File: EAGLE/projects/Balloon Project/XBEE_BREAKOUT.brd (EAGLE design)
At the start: 62.2 x 64.4 mm, 2 parts

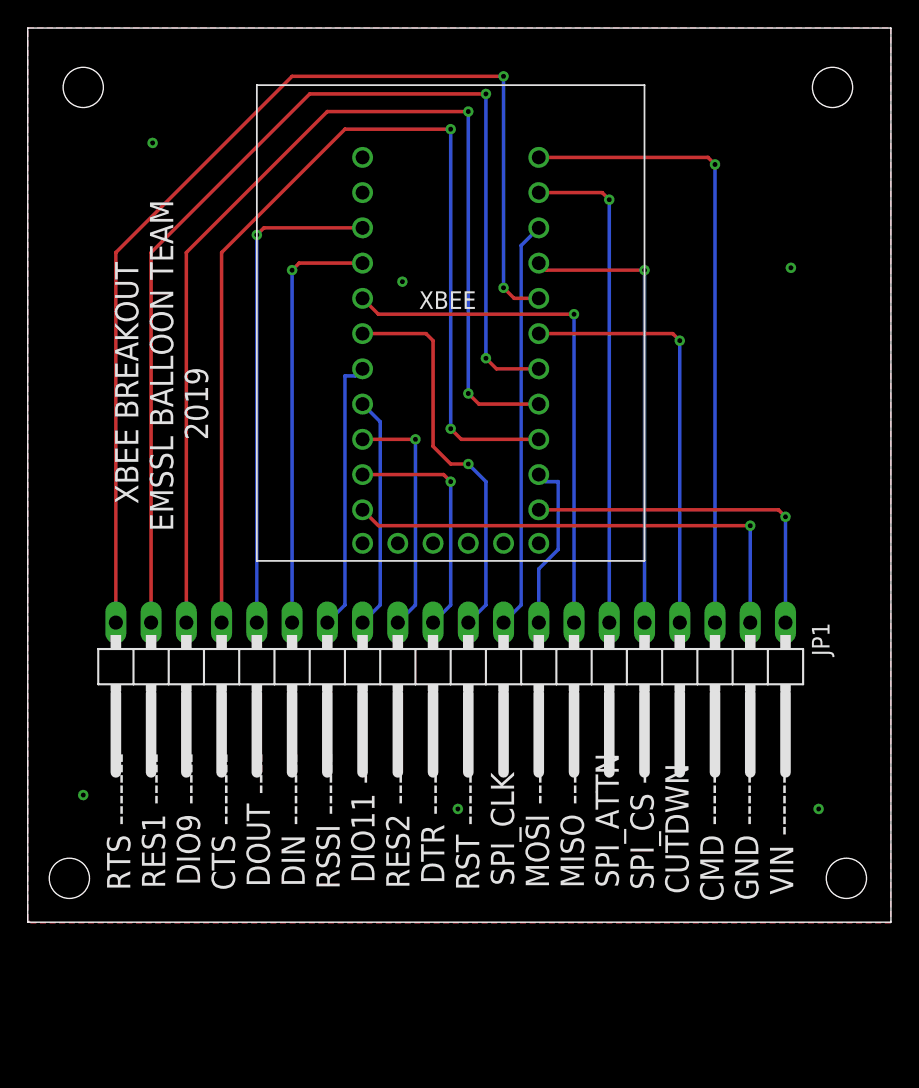
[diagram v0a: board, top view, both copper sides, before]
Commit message: optimized board layout - finished
-minimized vias
-optimized some routes
-added silkscreen to xbee
-ERC and DRC checks out for all boards
-ready for ordering
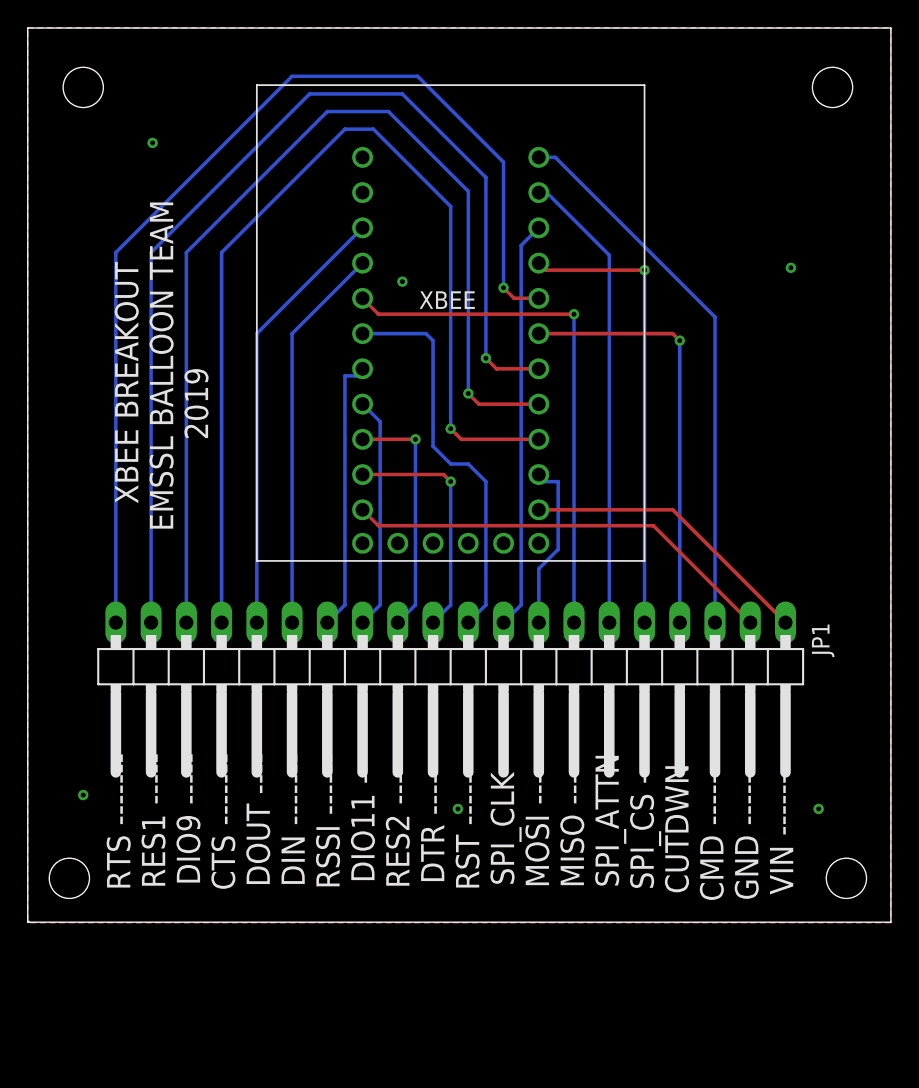
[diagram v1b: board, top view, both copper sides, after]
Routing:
- net XBEE_CMD_XBEE: track 45.9 -> 39.5 mm, vias 1 -> 0
- net 3V_XBEE: track 25.6 -> 21.1 mm, vias 1 -> 0
- net DOUT_XBEE: track 35.8 -> 31.6 mm, vias 1 -> 0
- net REG_GND_XBEE: track 35.4 -> 31.3 mm, vias 1 -> 6
- net RTS_XBEE: track 78.0 -> 74.3 mm, vias 2 -> 1
- net RES1_XBEE: track 78.7 -> 75.2 mm, vias 2 -> 1
- net DIO9_XBEE: track 76.9 -> 73.5 mm, vias 2 -> 1
- net CTS_XBEE: track 75.1 -> 71.9 mm, vias 2 -> 1
- net DIN_XBEE: track 30.7 -> 28.0 mm, vias 1 -> 0
- net XBEE_ATTN_XBEE: track 35.8 -> 33.4 mm, vias 1 -> 0
- net XBEE_RST_XBEE: vias 1 -> 0
